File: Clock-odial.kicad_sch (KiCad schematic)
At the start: 12 parts, among them J17 FPGA Bottom Shield SMS304

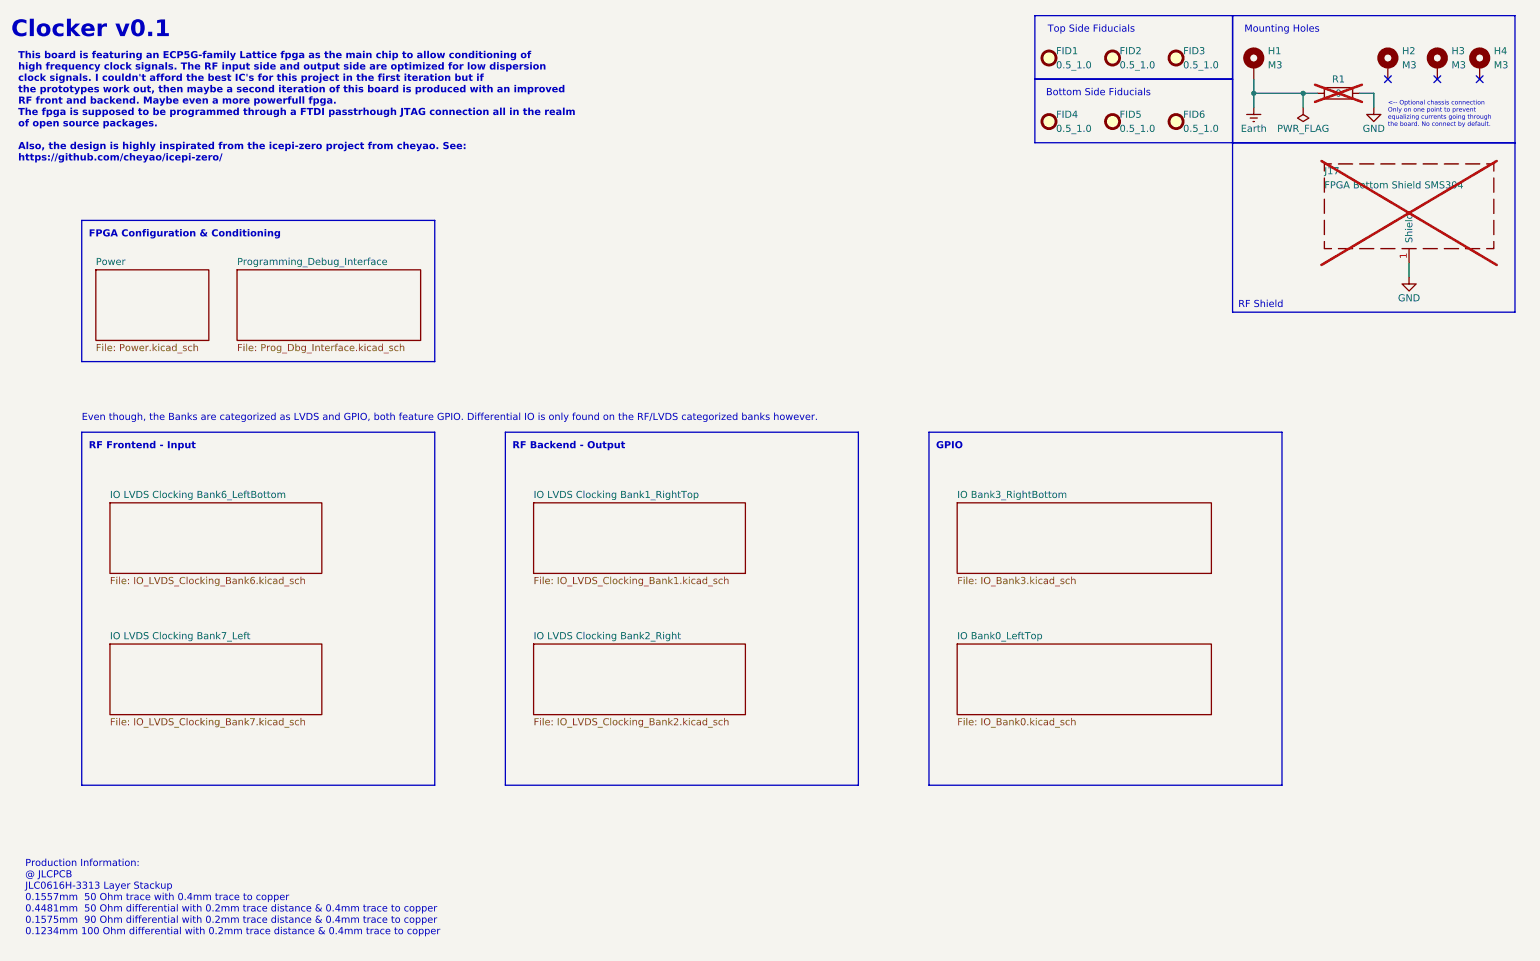
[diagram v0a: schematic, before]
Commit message: Document A bit and add more silkscreen
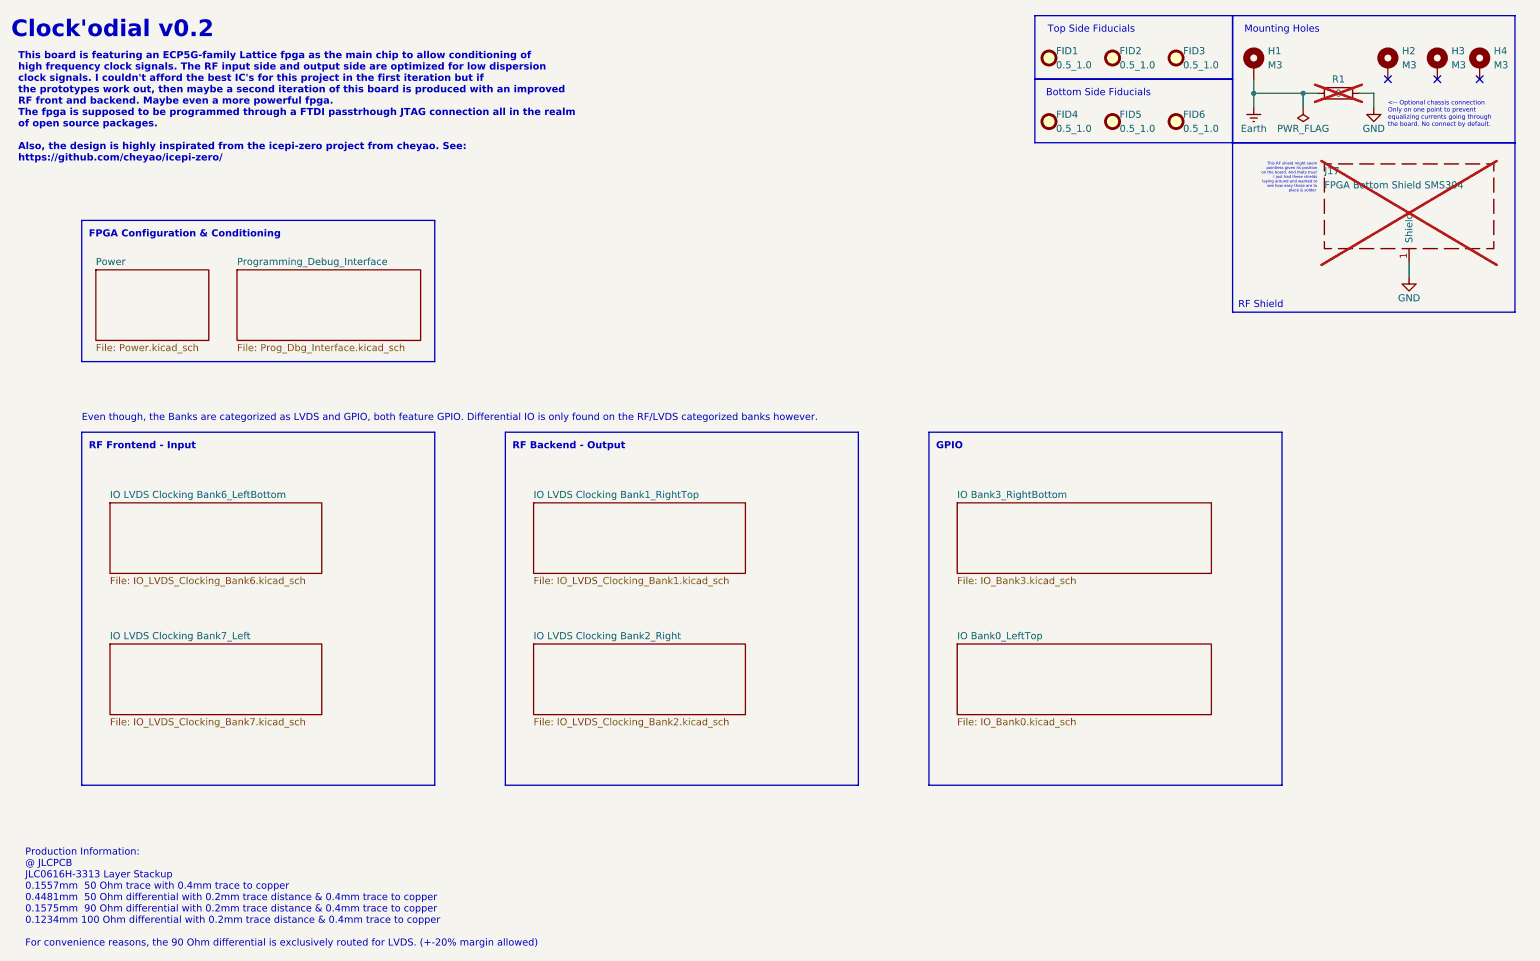
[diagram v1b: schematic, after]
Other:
- note added: "Clock'odial v0.2"
- note added: "Production Information: @ JLCPCB JLC0616H-3313 Layer Stackup 0.1557mm 50 Ohm trace with 0.4mm trace to copper 0.4481mm 50 Ohm differential with 0.2mm trace distance & 0.4mm trace to copper 0.1575mm 90 Ohm differential with 0.2mm trace distance & 0.4mm trace to copper 0.1234mm 100 Ohm differential with 0.2mm trace distance & 0.4mm trace to copper For convenience reasons, the 90 Ohm differential is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"
- note added: "This RF shield might seem pointless given its position on the board. And thats true! I just had these shields laying around and wanted to see how easy those are to place & solder."
- note removed: "Clocker v0.1"
- note removed: "Production Information: @ JLCPCB JLC0616H-3313 Layer Stackup 0.1557mm 50 Ohm trace with 0.4mm trace to copper 0.4481mm 50 Ohm differential with 0.2mm trace distance & 0.4mm trace to copper 0.1575mm 90 Ohm differential with 0.2mm trace distance & 0.4mm trace to copper 0.1234mm 100 Ohm differential with 0.2mm trace distance & 0.4mm trace to copper"
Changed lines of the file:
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@@
 		)
 	)
-	(text "Clocker v0.1"
+	(text "Clock'odial v0.2"
 		(exclude_from_sim no)
 		(at 12.7 16.51 0)
@@
 		)
 	)
-	(text "This board is featuring an ECP5G-family Lattice fpga as the main chip to allow conditioning of\nhigh frequency clock signals. The RF input side and output side are optimized for low dispersion\nclock signals. I couldn't afford the best IC's for this project in the first iteration but if\nthe prototypes work out, then maybe a second iteration of this board is produced with an improved\nRF front and backend. Maybe even a more powerfull fpga.\nThe fpga is supposed to be programmed through a FTDI passtrhough JTAG connection all in the realm\nof open source packages.\n\nAlso, the design is highly inspirated from the icepi-zero project from cheyao. See:\nhttps://github.com/cheyao/icepi-zero/\n"
+	(text "This board is featuring an ECP5G-family Lattice fpga as the main chip to allow conditioning of\nhigh frequency clock signals. The RF input side and output side are optimized for low dispersion\nclock signals. I couldn't afford the best IC's for this project in the first iteration but if\nthe prototypes work out, then maybe a second iteration of this board is produced with an improved\nRF front and backend. Maybe even a more powerful fpga.\nThe fpga is supposed to be programmed through a FTDI passtrhough JTAG connection all in the realm\nof open source packages.\n\nAlso, the design is highly inspirated from the icepi-zero project from cheyao. See:\nhttps://github.com/cheyao/icepi-zero/\n"
 		(exclude_from_sim no)
 		(at 13.97 30.48 0)
@@
 		)
 	)
-	(text "Production Information:\n@ JLCPCB\nJLC0616H-3313 Layer Stackup\n0.1557mm  50 Ohm trace with 0.4mm trace to copper\n0.4481mm  50 Ohm differential with 0.2mm trace distance & 0.4mm trace to copper\n0.1575mm  90 Ohm differential with 0.2mm trace distance & 0.4mm trace to copper\n0.1234mm 100 Ohm differential with 0.2mm trace distance & 0.4mm trace to copper"
+	(text "Production Information:\n@ JLCPCB\nJLC0616H-3313 Layer Stackup\n0.1557mm  50 Ohm trace with 0.4mm trace to copper\n0.4481mm  50 Ohm differential with 0.2mm trace distance & 0.4mm trace to copper\n0.1575mm  90 Ohm differential with 0.2mm trace distance & 0.4mm trace to copper\n0.1234mm 100 Ohm differential with 0.2mm trace distance & 0.4mm trace to copper\n\nFor convenience reasons, the 90 Ohm differential is exclusively routed for LVDS. (+-20% margin allowed)"
 		(exclude_from_sim no)
 		(at 15.24 172.72 0)
@@
 		)
 	)
+	(text "This RF shield might seem\npointless given its position\non the board. And thats true!\nI just had these shields\nlaying around and wanted to\nsee how easy those are to\nplace & solder."
+		(exclude_from_sim no)
+		(at 247.65 43.18 0)
+		(effects
+			(font
+				(size 0.5 0.5)
+			)
+			(justify right)
+		)
+	)
